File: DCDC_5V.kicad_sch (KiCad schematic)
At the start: 12 parts, among them U10 TPS563200

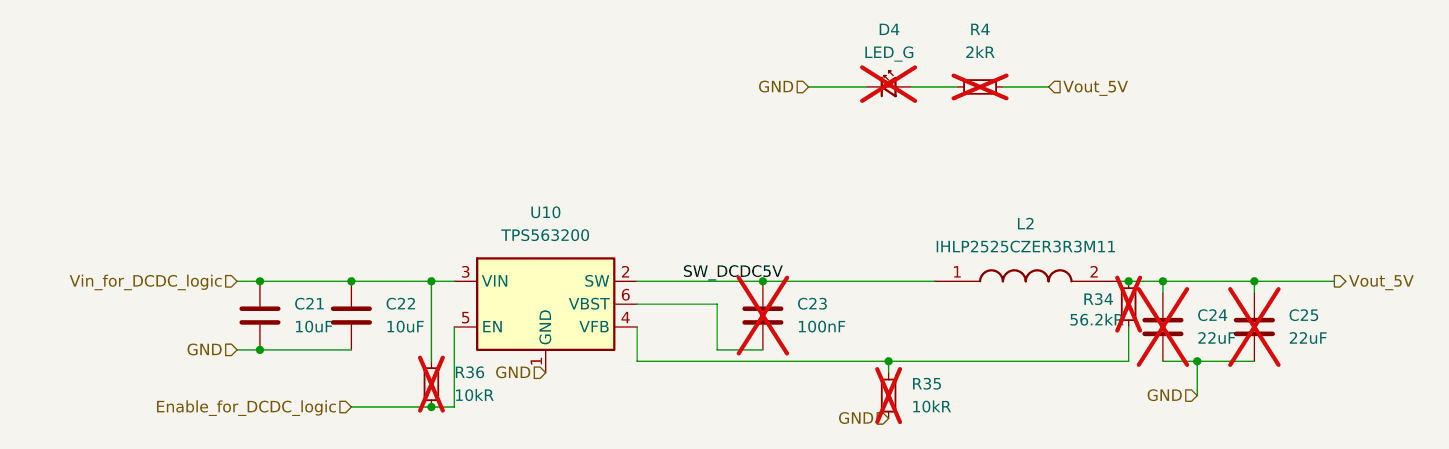
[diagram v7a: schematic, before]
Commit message: fix DNP (was just for checking what was to be bought)
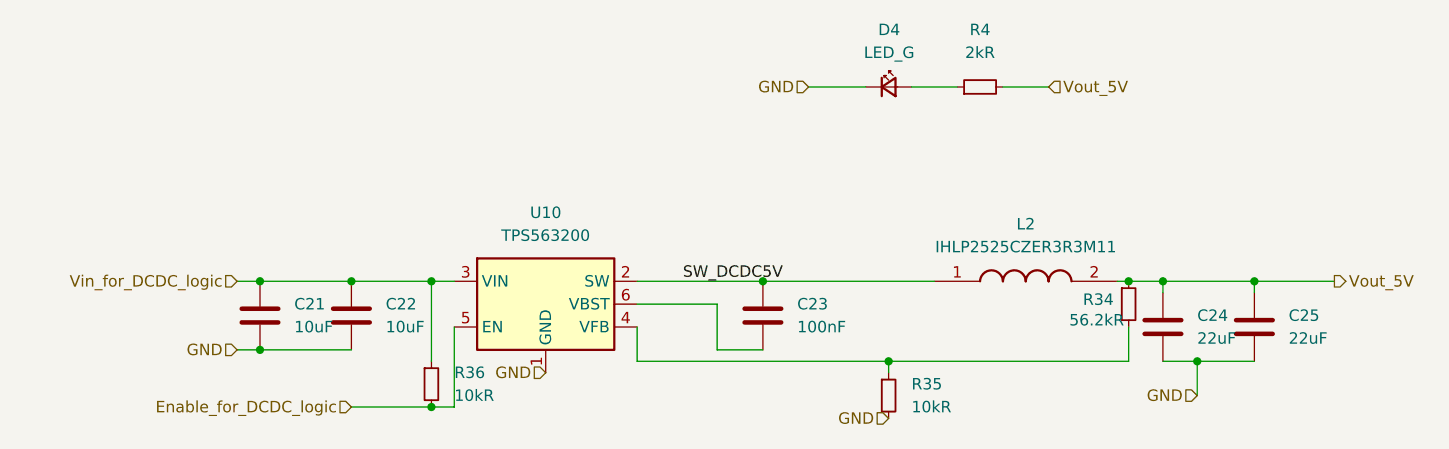
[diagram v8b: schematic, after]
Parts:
- C23, C24, C25, D4, R34, R35, R36, R4: now fitted
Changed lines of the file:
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@@
 		(in_bom yes)
 		(on_board yes)
-		(dnp yes)
+		(dnp no)
 		(property "Reference" "R34"
 			(at 179.07 76.962 0)
@@
 		(in_bom yes)
 		(on_board yes)
-		(dnp yes)
+		(dnp no)
 		(fields_autoplaced yes)
 		(property "Reference" "C24"
@@
 		(in_bom yes)
 		(on_board yes)
-		(dnp yes)
+		(dnp no)
 		(fields_autoplaced yes)
 		(property "Reference" "R36"
@@
 		(in_bom yes)
 		(on_board yes)
-		(dnp yes)
+		(dnp no)
 		(fields_autoplaced yes)
 		(property "Reference" "C25"
@@
 		(in_bom yes)
 		(on_board yes)
-		(dnp yes)
+		(dnp no)
 		(fields_autoplaced yes)
 		(property "Reference" "D4"
@@
 		(in_bom yes)
 		(on_board yes)
-		(dnp yes)
+		(dnp no)
 		(fields_autoplaced yes)
 		(property "Reference" "R4"
@@
 		(in_bom yes)
 		(on_board yes)
-		(dnp yes)
+		(dnp no)
 		(fields_autoplaced yes)
 		(property "Reference" "C23"
@@
 		(in_bom yes)
 		(on_board yes)
-		(dnp yes)
+		(dnp no)
 		(fields_autoplaced yes)
 		(property "Reference" "R35"
